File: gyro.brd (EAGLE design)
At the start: 15.2 x 15.2 mm, 9 parts, among them IC2 LGD20H

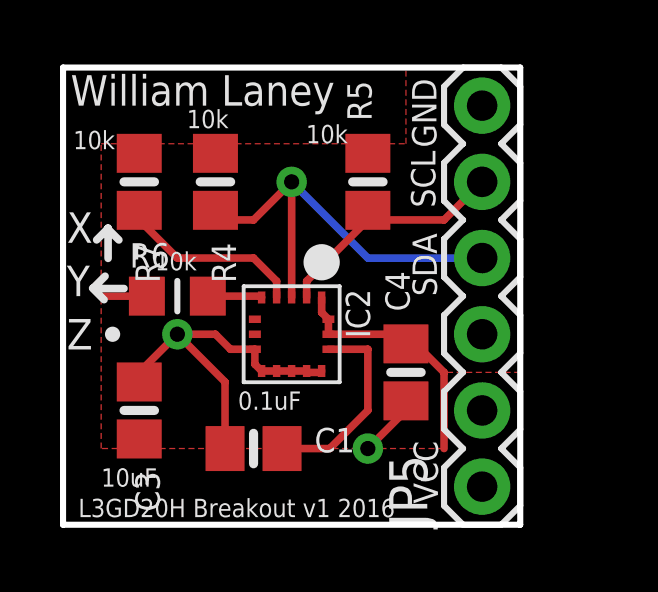
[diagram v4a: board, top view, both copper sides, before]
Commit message: set up pins to line up with accel corectly
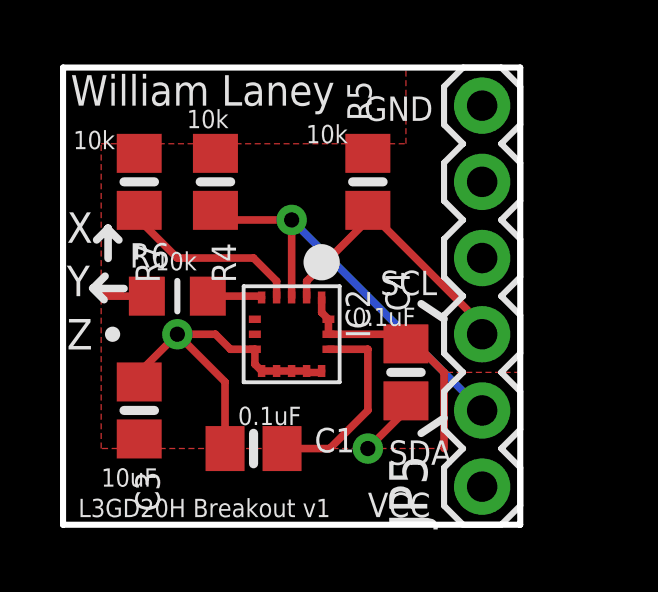
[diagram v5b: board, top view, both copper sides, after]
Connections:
- net SCL: now also JP5.3; no longer JP5.5
- net SDA: now also JP5.2; no longer JP5.4
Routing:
- net SCL: track 8.09 -> 9.46 mm
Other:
- board text added: "L3GD20H Breakout v1"
- board text removed: "L3GD20H Breakout v1 2016"
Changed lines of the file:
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@@
 <wire x1="0" y1="0" x2="15.24" y2="0" width="0.2032" layer="20"/>
 <wire x1="15.24" y1="0" x2="15.24" y2="15.24" width="0.2032" layer="20"/>
-<text x="11.684" y="2.794" size="0.8128" layer="21" ratio="15" rot="R270">VCC</text>
-<text x="12.446" y="12.573" size="0.8128" layer="21" ratio="15" rot="R90">GND</text>
-<text x="12.46281875" y="7.62" size="0.8128" layer="21" ratio="15" rot="R90">SDA</text>
-<text x="11.599478125" y="12.4685375" size="0.8128" layer="21" ratio="15" rot="R270">SCL</text>
+<text x="10.16" y="0.254" size="0.8128" layer="21" ratio="15">VCC</text>
+<text x="10.033" y="13.462" size="0.8128" layer="21" ratio="15">GND</text>
+<text x="12.954" y="2.81081875" size="0.8128" layer="21" ratio="15" rot="R180">SDA</text>
+<text x="12.4685375" y="8.466521875" size="0.8128" layer="21" ratio="15" rot="R180">SCL</text>
 <text x="1.27" y="1.27" size="0.6096" layer="21" ratio="15">10uF</text>
-<text x="5.831621875" y="3.832565625" size="0.6096" layer="21" ratio="15">0.1uF</text>
+<text x="5.831621875" y="3.324565625" size="0.6096" layer="21" ratio="15">0.1uF</text>
 <wire x1="1.5014625" y1="8.878928125" x2="1.5014625" y2="9.894928125" width="0.254" layer="21"/>
 <circle x="1.651" y="6.35" radius="0.127" width="0.254" layer="21"/>
@@
 <text x="0.338071875" y="12.51946875" size="0.6096" layer="21" ratio="15">10k</text>
 <text x="0.254" y="13.97" size="1.016" layer="21">William Laney</text>
-<text x="0.508" y="0.254" size="0.6096" layer="21">L3GD20H Breakout v1 2016</text>
+<text x="0.508" y="0.254" size="0.6096" layer="21">L3GD20H Breakout v1</text>
 <text x="4.124471875" y="13.2190375" size="0.6096" layer="21" ratio="15">10k</text>
 <text x="8.09798125" y="12.716803125" size="0.6096" layer="21" ratio="15">10k</text>
 <text x="3.06518125" y="8.4800375" size="0.6096" layer="21" ratio="15">10k</text>
+<text x="9.641621875" y="6.626565625" size="0.6096" layer="21" ratio="15">0.1uF</text>
+<wire x1="11.938" y1="7.366" x2="12.7" y2="6.858" width="0.254" layer="21"/>
+<wire x1="12.7" y1="3.556" x2="11.938" y2="3.048" width="0.254" layer="21"/>
 </plain>
 <attributes>
@@
 <contactref element="R4" pad="2"/>
 <contactref element="IC2" pad="3"/>
-<via x="7.62" y="11.43" extent="1-16" drill="0.508"/>
-<wire x1="7.62" y1="11.43" x2="7.62" y2="7.575" width="0.254" layer="1"/>
+<contactref element="JP5" pad="2"/>
+<wire x1="13.97" y1="3.81" x2="7.62" y2="10.16" width="0.254" layer="16"/>
+<via x="7.62" y="10.16" extent="1-16" drill="0.508"/>
+<wire x1="7.62" y1="10.16" x2="5.4" y2="10.16" width="0.254" layer="1"/>
 <wire x1="5.4" y1="10.16" x2="5.08" y2="10.48" width="0.254" layer="1"/>
-<wire x1="5.4" y1="10.16" x2="6.35" y2="10.16" width="0.254" layer="1"/>
-<wire x1="6.35" y1="10.16" x2="7.62" y2="11.43" width="0.254" layer="1"/>
-<contactref element="JP5" pad="4"/>
-<wire x1="13.97" y1="8.89" x2="10.16" y2="8.89" width="0.254" layer="16"/>
-<wire x1="10.16" y1="8.89" x2="7.62" y2="11.43" width="0.254" layer="16"/>
+<wire x1="7.62" y1="10.16" x2="7.62" y2="7.575" width="0.254" layer="1"/>
 </signal>
 <signal name="SCL">
 <contactref element="IC2" pad="2"/>
 <contactref element="R5" pad="1"/>
-<contactref element="JP5" pad="5"/>
-<wire x1="10.16" y1="10.16" x2="12.7" y2="10.16" width="0.254" layer="1"/>
-<wire x1="12.7" y1="10.16" x2="13.97" y2="11.43" width="0.254" layer="1"/>
 <wire x1="10.16" y1="10.16" x2="8.12" y2="8.12" width="0.254" layer="1"/>
 <wire x1="8.12" y1="7.575" x2="8.12" y2="8.12" width="0.254" layer="1"/>
 <wire x1="10.16" y1="10.16" x2="10.16" y2="10.48" width="0.254" layer="1"/>
+<contactref element="JP5" pad="3"/>
+<wire x1="13.97" y1="6.35" x2="13.97" y2="6.67" width="0.254" layer="1"/>
+<wire x1="13.97" y1="6.67" x2="10.16" y2="10.48" width="0.254" layer="1"/>
 </signal>
 <signal name="CS_3.3V">
